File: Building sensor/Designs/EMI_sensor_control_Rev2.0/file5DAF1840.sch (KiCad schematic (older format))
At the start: 32 parts, among them U11 INA163UA_2K5, U12 ADA4096-2ARMZ, U13 INA163UA_2K5

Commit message: Back up
Backup of rev 2.0 for board
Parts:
- removed C43, C89: C 100n, Capacitor_Tantalum_SMD:CP_EIA-3216-18_Kemet-A_Pad1.58x1.35mm_HandSolder, symbol Device:C_Small
- removed L5: L 1.2u, footprints:AISC-1008-1R2G-T, symbol Device:L
- removed R41: R 47, Resistor_SMD:R_1206_3216Metric_Pad1.42x1.75mm_HandSolder, symbol Device:R
- removed R45: R 22ohm, Resistor_SMD:R_0805_2012Metric_Pad1.15x1.40mm_HandSolder, symbol Device:R
- removed U13: INA163UA_2K5, footprints:INA163UA&slash_2K5, symbol 2019-07-16_16-02-38:INA163UA_2K5
- added C? (x2): C 100n, Capacitor_Tantalum_SMD:CP_EIA-3216-18_Kemet-A_Pad1.58x1.35mm_HandSolder, symbol Device:C_Small
- added L? (x2): L 1.2u, footprints:AISC-1008-1R2G-T, symbol Device:L
- added R?: R 22ohm, Resistor_SMD:R_0805_2012Metric_Pad1.15x1.40mm_HandSolder, symbol Device:R
- added R? (x2): R 47, Resistor_SMD:R_1206_3216Metric_Pad1.42x1.75mm_HandSolder, symbol Device:R
- added U?: INA163UA_2K5, footprints:INA163UA&slash_2K5, symbol 2019-07-16_16-02-38:INA163UA_2K5
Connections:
- net +5V: now also C?.1, U?.11 (+V)
- net -5V: now also C?.1, U?.6 (-V)
- net BxCoilAmp: now also U?.8 (SENSE), U?.9 (VO)
- net GND: now also C?.2, C?.2, U?.10 (REF); no longer AE2.2
- net BxCoilsig renamed Bx_High
- net Bx_High: now also L?.1, R?.2; no longer L3.1, R33.2
- net RxCoilsig+ renamed Rx_Low
- net Rx_Low: now also AE2.2, L?.2, R?.2; no longer AE3.1
- new net: R?.1, U?.12 (GS2)
- new net: R?.2, U?.3 (GS1)
- new net: L?.2, R?.1, U?.4 (-VIN)
- new net: L?.1, R?.1, U?.5 (+VIN)
- new net Rx_High: AE3.1, L3.1, R33.2

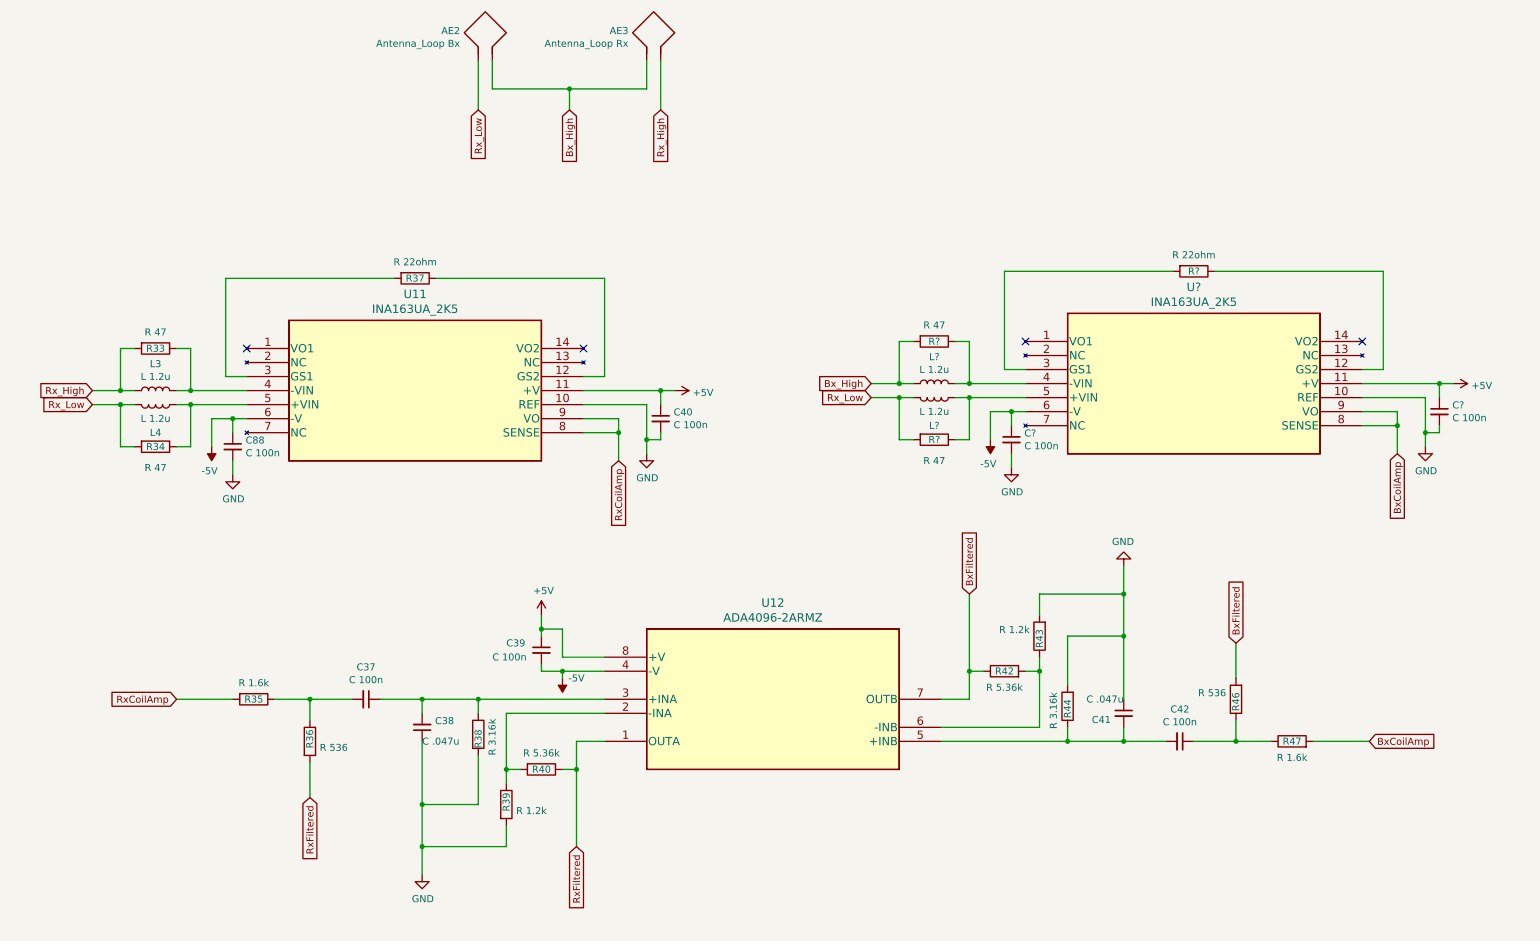
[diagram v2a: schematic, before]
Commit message: Rev 2.0 Complete
Rev 2.0 of PCB Completed
SCHM, PCB layout, and gerber files generated
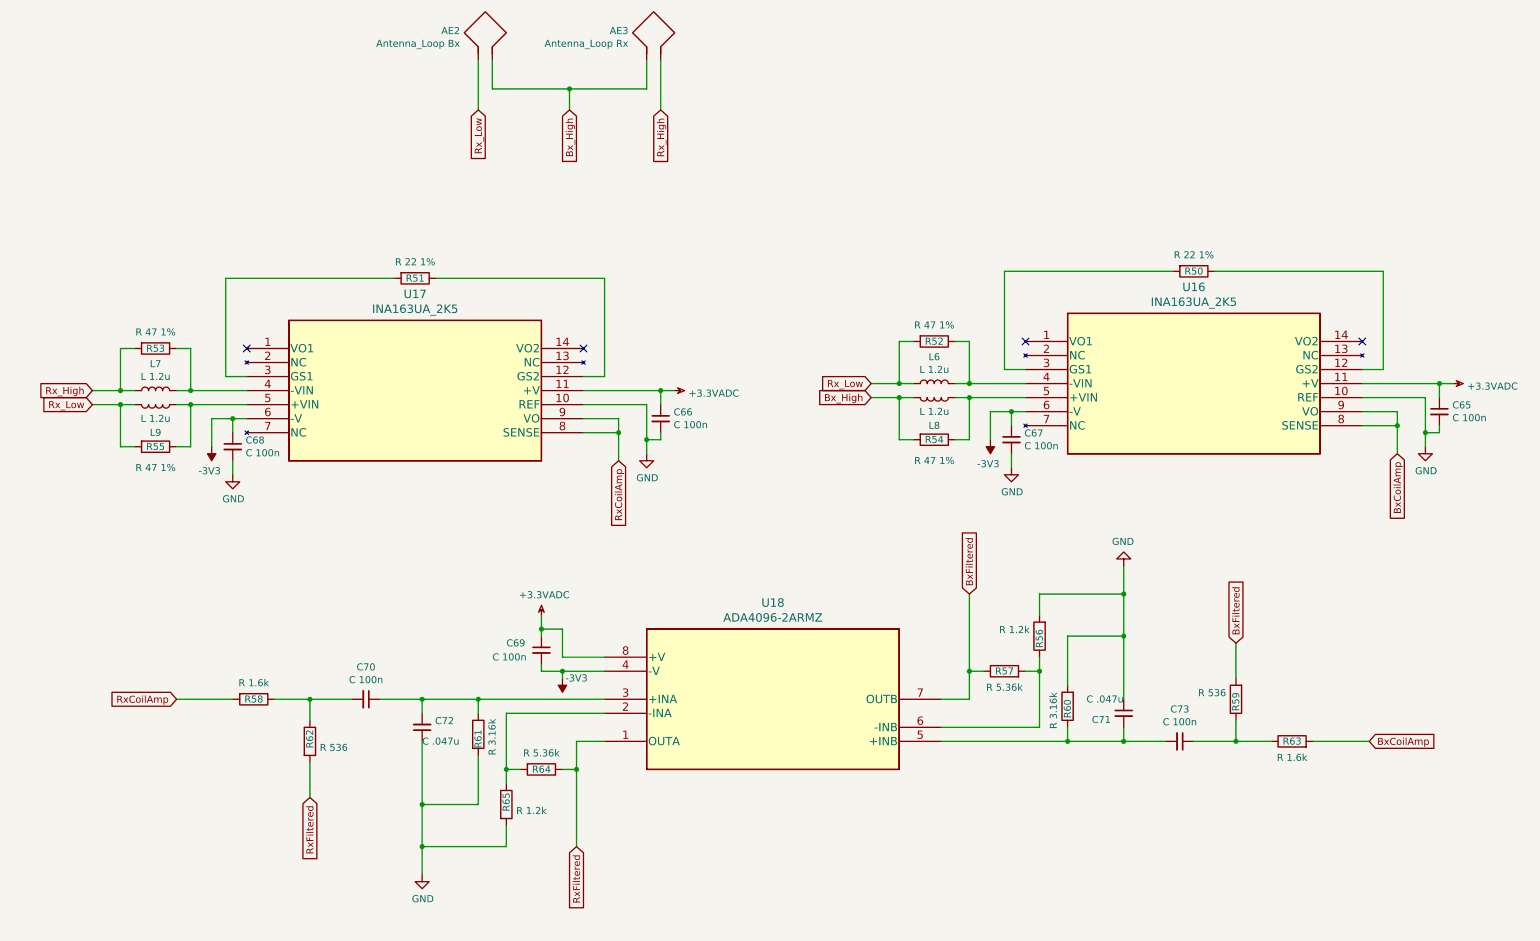
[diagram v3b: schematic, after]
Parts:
- L6, L8: renamed from L?; footprint footprints:AISC-1008-1R2G-T -> Inductor_SMD:L_0805_2012Metric_Pad1.15x1.40mm_HandSolder
- L7: renamed from L3; footprint footprints:AISC-1008-1R2G-T -> Inductor_SMD:L_0805_2012Metric_Pad1.15x1.40mm_HandSolder
- L9: renamed from L4; footprint footprints:AISC-1008-1R2G-T -> Inductor_SMD:L_0805_2012Metric_Pad1.15x1.40mm_HandSolder
- R50: renamed from R?; value R 22ohm -> R 22 1%; footprint Resistor_SMD:R_0805_2012Metric_Pad1.15x1.40mm_HandSolder -> Resistor_SMD:R_1206_3216Metric_Pad1.42x1.75mm_HandSolder
- R51: renamed from R37; value R 22ohm -> R 22 1%; footprint Resistor_SMD:R_0805_2012Metric_Pad1.15x1.40mm_HandSolder -> Resistor_SMD:R_1206_3216Metric_Pad1.42x1.75mm_HandSolder
- R52, R54: renamed from R?; value R 47 -> R 47 1%
- R53: renamed from R33; value R 47 -> R 47 1%
- R55: renamed from R34; value R 47 -> R 47 1%
- U16: renamed from U?; footprint footprints:INA163UA&slash_2K5 -> Package_SO:SOIC-14_3.9x8.7mm_P1.27mm
- U17: renamed from U11; footprint footprints:INA163UA&slash_2K5 -> Package_SO:SOIC-14_3.9x8.7mm_P1.27mm
- U18: renamed from U12; footprint footprints:ADA4096-2ARMZ -> Package_SO:MSOP-8_3x3mm_P0.65mm
- gave numbers to parts that had none: 2
- renumbered C40 to C66, C88 to C68, C39 to C69, C37 to C70, C41 to C71, C38 to C72, C42 to C73, R43 to R56, R42 to R57, R35 to R58, R46 to R59, R44 to R60, R38 to R61, R36 to R62, R47 to R63, R40 to R64, R39 to R65
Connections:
- net Bx_High: now also L8.2, R54.2; no longer L6.1, R52.2
- net Rx_Low: now also L6.1, R52.2; no longer L8.2, R54.2
- net +5V renamed +3.3VADC
- net -5V renamed -3V3
